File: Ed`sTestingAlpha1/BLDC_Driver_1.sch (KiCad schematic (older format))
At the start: 0 parts

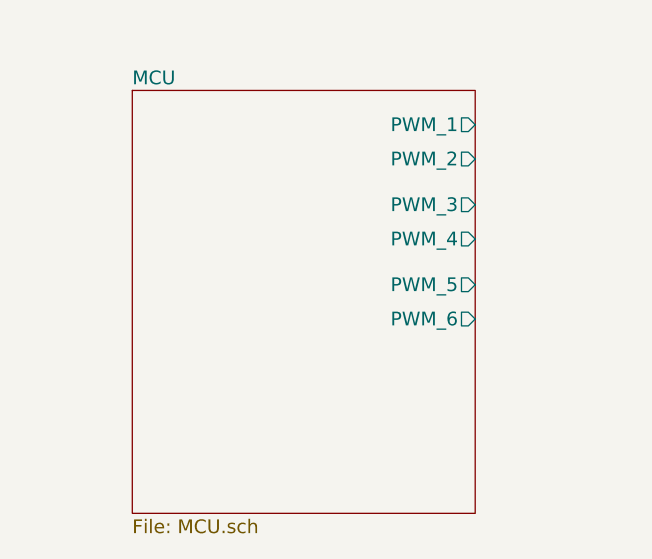
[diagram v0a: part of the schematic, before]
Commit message: Small mods on schematic -- added some pins
Added some docs
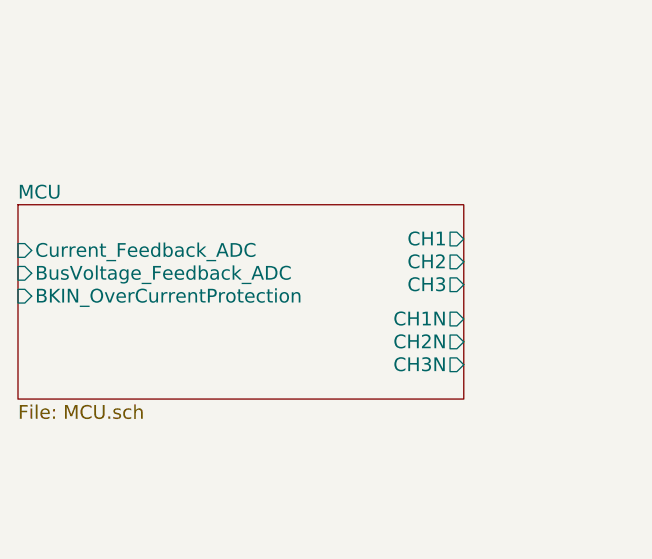
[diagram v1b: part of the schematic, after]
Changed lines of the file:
@@
 EESchema Schematic File Version 2
+LIBS:BLDC_Driver_1-rescue
 LIBS:power
 LIBS:device
@@
 $EndDescr
 $Sheet
-S 2000 2900 1500 1850
+S 1500 3400 1950 850
 U 582DDEF5
 F0 "MCU" 60
 F1 "MCU.sch" 60
-F2 "PWM_1" O R 3500 3050 60
-F3 "PWM_2" O R 3500 3200 60
-F4 "PWM_3" O R 3500 3400 60
-F5 "PWM_4" O R 3500 3550 60
-F6 "PWM_5" O R 3500 3750 60
-F7 "PWM_6" O R 3500 3900 60
+F2 "CH1" O R 3450 3550 60
+F3 "CH2" O R 3450 3650 60
+F4 "CH3" O R 3450 3750 60
+F5 "CH1N" O R 3450 3900 60
+F6 "CH2N" O R 3450 4000 60
+F7 "CH3N" O R 3450 4100 60
+F8 "Current_Feedback_ADC" I L 1500 3600 60
+F9 "BusVoltage_Feedback_ADC" I L 1500 3700 60
+F10 "BKIN_OverCurrentProtection" I L 1500 3800 60
 $EndSheet
 $Sheet
